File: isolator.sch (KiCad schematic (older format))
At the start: 3 parts, among them U1 Si8640BB-B-IS1

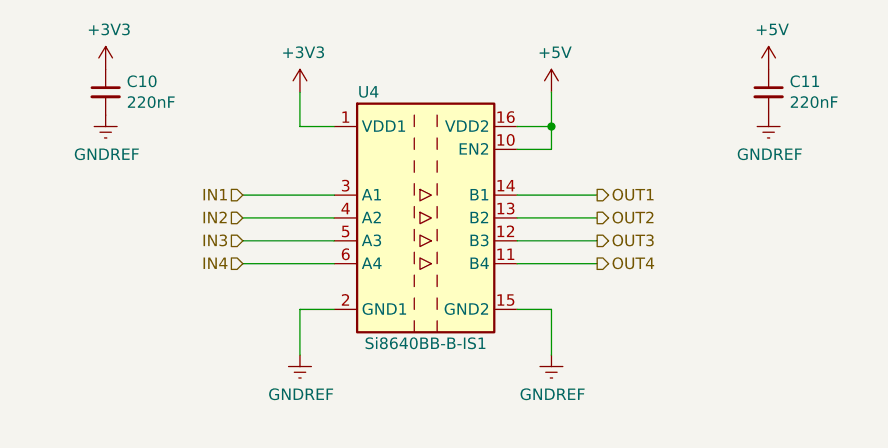
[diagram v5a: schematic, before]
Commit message: Continued layouting
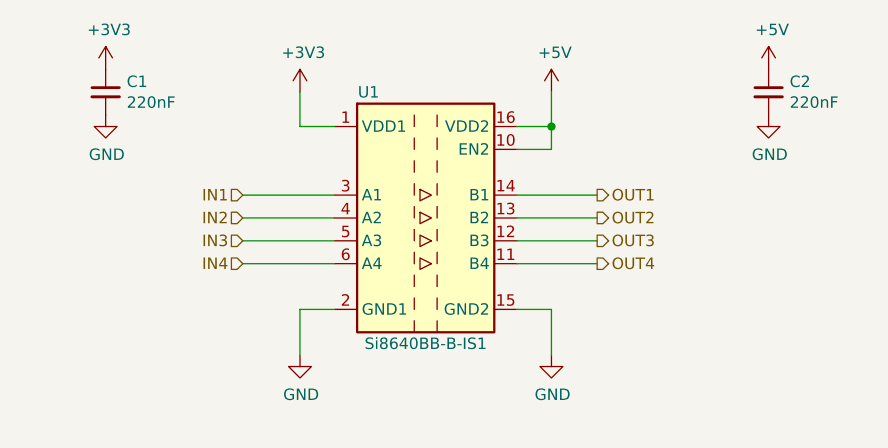
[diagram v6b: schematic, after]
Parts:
- renumbered C4 to C1, C5 to C2
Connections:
- net GNDREF renamed GND
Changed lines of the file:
@@
 P 5200 3500
 AR Path="/5BCC578B/5BCC7CBC" Ref="U1"  Part="1"
-AR Path="/5BCC79AE/5BCC7CBC" Ref="U3"  Part="1"
-AR Path="/5BCC7A96/5BCC7CBC" Ref="U2"  Part="1"
-AR Path="/5BCC8BB7/5BCC7CBC" Ref="U4"  Part="1"
-F 0 "U4" H 4950 4050 50  0000 C CNN
+AR Path="/5BCC79AE/5BCC7CBC" Ref="U4"  Part="1"
+AR Path="/5BCC7A96/5BCC7CBC" Ref="U3"  Part="1"
+AR Path="/5BCC8BB7/5BCC7CBC" Ref="U5"  Part="1"
+F 0 "U1" H 4950 4050 50  0000 C CNN
 F 1 "Si8640BB-B-IS1" H 5200 2950 50  0000 C CNN
 F 2 "Package_SO:SOIC-16_3.9x9.9mm_P1.27mm" H 5200 2950 50  0001 C CIN
@@
 $EndComp
 $Comp
-L power:GNDREF #PWR0105
-U 1 1 5BCC7D47
-P 4650 4100
-AR Path="/5BCC578B/5BCC7D47" Ref="#PWR0105"  Part="1"
-AR Path="/5BCC79AE/5BCC7D47" Ref="#PWR0118"  Part="1"
-AR Path="/5BCC7A96/5BCC7D47" Ref="#PWR0114"  Part="1"
-AR Path="/5BCC8BB7/5BCC7D47" Ref="#PWR0122"  Part="1"
-F 0 "#PWR0122" H 4650 3850 50  0001 C CNN
-F 1 "GNDREF" H 4655 3927 50  0000 C CNN
-F 2 "" H 4650 4100 50  0001 C CNN
-F 3 "" H 4650 4100 50  0001 C CNN
-	1    4650 4100
-	1    0    0    -1
-$EndComp
-$Comp
-L power:GNDREF #PWR0106
-U 1 1 5BCC7D5B
-P 5750 4100
-AR Path="/5BCC578B/5BCC7D5B" Ref="#PWR0106"  Part="1"
-AR Path="/5BCC79AE/5BCC7D5B" Ref="#PWR0119"  Part="1"
-AR Path="/5BCC7A96/5BCC7D5B" Ref="#PWR0115"  Part="1"
-AR Path="/5BCC8BB7/5BCC7D5B" Ref="#PWR0123"  Part="1"
-F 0 "#PWR0123" H 5750 3850 50  0001 C CNN
-F 1 "GNDREF" H 5755 3927 50  0000 C CNN
-F 2 "" H 5750 4100 50  0001 C CNN
-F 3 "" H 5750 4100 50  0001 C CNN
-	1    5750 4100
-	1    0    0    -1
-$EndComp
-$Comp
-L power:+3V3 #PWR0107
+L power:+3V3 #PWR07
 U 1 1 5BCC7DB8
 P 4650 2950
-AR Path="/5BCC578B/5BCC7DB8" Ref="#PWR0107"  Part="1"
-AR Path="/5BCC79AE/5BCC7DB8" Ref="#PWR0120"  Part="1"
-AR Path="/5BCC7A96/5BCC7DB8" Ref="#PWR0116"  Part="1"
-AR Path="/5BCC8BB7/5BCC7DB8" Ref="#PWR0124"  Part="1"
-F 0 "#PWR0124" H 4650 2800 50  0001 C CNN
+AR Path="/5BCC578B/5BCC7DB8" Ref="#PWR07"  Part="1"
+AR Path="/5BCC79AE/5BCC7DB8" Ref="#PWR028"  Part="1"
+AR Path="/5BCC7A96/5BCC7DB8" Ref="#PWR020"  Part="1"
+AR Path="/5BCC8BB7/5BCC7DB8" Ref="#PWR036"  Part="1"
+F 0 "#PWR07" H 4650 2800 50  0001 C CNN
 F 1 "+3V3" H 4665 3123 50  0000 C CNN
 F 2 "" H 4650 2950 50  0001 C CNN
@@
 $EndComp
 $Comp
-L power:+5V #PWR0108
+L power:+5V #PWR09
 U 1 1 5BCC7E07
 P 5750 2950
-AR Path="/5BCC578B/5BCC7E07" Ref="#PWR0108"  Part="1"
-AR Path="/5BCC79AE/5BCC7E07" Ref="#PWR0121"  Part="1"
-AR Path="/5BCC7A96/5BCC7E07" Ref="#PWR0117"  Part="1"
-AR Path="/5BCC8BB7/5BCC7E07" Ref="#PWR0125"  Part="1"
-F 0 "#PWR0125" H 5750 2800 50  0001 C CNN
+AR Path="/5BCC578B/5BCC7E07" Ref="#PWR09"  Part="1"
+AR Path="/5BCC79AE/5BCC7E07" Ref="#PWR030"  Part="1"
+AR Path="/5BCC7A96/5BCC7E07" Ref="#PWR022"  Part="1"
+AR Path="/5BCC8BB7/5BCC7E07" Ref="#PWR038"  Part="1"
+F 0 "#PWR09" H 5750 2800 50  0001 C CNN
 F 1 "+5V" H 5765 3123 50  0000 C CNN
 F 2 "" H 5750 2950 50  0001 C CNN
@@
 	5750 2950 5750 3100
 $Comp
-L power:+3V3 #PWR01
+L power:+3V3 #PWR05
 U 1 1 5BCCF224
 P 3800 2850
-AR Path="/5BCC578B/5BCCF224" Ref="#PWR01"  Part="1"
-AR Path="/5BCC79AE/5BCCF224" Ref="#PWR09"  Part="1"
-AR Path="/5BCC7A96/5BCCF224" Ref="#PWR05"  Part="1"
-AR Path="/5BCC8BB7/5BCCF224" Ref="#PWR013"  Part="1"
-F 0 "#PWR013" H 3800 2700 50  0001 C CNN
+AR Path="/5BCC578B/5BCCF224" Ref="#PWR05"  Part="1"
+AR Path="/5BCC79AE/5BCCF224" Ref="#PWR026"  Part="1"
+AR Path="/5BCC7A96/5BCCF224" Ref="#PWR018"  Part="1"
+AR Path="/5BCC8BB7/5BCCF224" Ref="#PWR034"  Part="1"
+F 0 "#PWR05" H 3800 2700 50  0001 C CNN
 F 1 "+3V3" H 3815 3023 50  0000 C CNN
 F 2 "" H 3800 2850 50  0001 C CNN
@@
 $EndComp
 $Comp
-L Device:C_Small C4
+L Device:C_Small C1
 U 1 1 5BCCF242
 P 3800 2950
-AR Path="/5BCC578B/5BCCF242" Ref="C4"  Part="1"
+AR Path="/5BCC578B/5BCCF242" Ref="C1"  Part="1"
 AR Path="/5BCC79AE/5BCCF242" Ref="C8"  Part="1"
 AR Path="/5BCC7A96/5BCCF242" Ref="C6"  Part="1"
 AR Path="/5BCC8BB7/5BCCF242" Ref="C10"  Part="1"
-F 0 "C10" H 3892 2996 50  0000 L CNN
+F 0 "C1" H 3892 2996 50  0000 L CNN
 F 1 "220nF" H 3892 2905 50  0000 L CNN
 F 2 "Capacitor_SMD:C_0805_2012Metric_Pad1.15x1.40mm_HandSolder" H 3800 2950 50  0001 C CNN
@@
 $EndComp
 $Comp
-L power:GNDREF #PWR02
-U 1 1 5BCCF276
-P 3800 3050
-AR Path="/5BCC578B/5BCCF276" Ref="#PWR02"  Part="1"
-AR Path="/5BCC79AE/5BCCF276" Ref="#PWR010"  Part="1"
-AR Path="/5BCC7A96/5BCCF276" Ref="#PWR06"  Part="1"
-AR Path="/5BCC8BB7/5BCCF276" Ref="#PWR014"  Part="1"
-F 0 "#PWR014" H 3800 2800 50  0001 C CNN
-F 1 "GNDREF" H 3805 2877 50  0000 C CNN
-F 2 "" H 3800 3050 50  0001 C CNN
-F 3 "" H 3800 3050 50  0001 C CNN
-	1    3800 3050
-	1    0    0    -1
-$EndComp
-$Comp
-L Device:C_Small C5
+L Device:C_Small C2
 U 1 1 5BCCF2B7
 P 6700 2950
-AR Path="/5BCC578B/5BCCF2B7" Ref="C5"  Part="1"
+AR Path="/5BCC578B/5BCCF2B7" Ref="C2"  Part="1"
 AR Path="/5BCC79AE/5BCCF2B7" Ref="C9"  Part="1"
 AR Path="/5BCC7A96/5BCCF2B7" Ref="C7"  Part="1"
 AR Path="/5BCC8BB7/5BCCF2B7" Ref="C11"  Part="1"
-F 0 "C11" H 6792 2996 50  0000 L CNN
+F 0 "C2" H 6792 2996 50  0000 L CNN
 F 1 "220nF" H 6792 2905 50  0000 L CNN
 F 2 "Capacitor_SMD:C_0805_2012Metric_Pad1.15x1.40mm_HandSolder" H 6700 2950 50  0001 C CNN
@@
 $EndComp
 $Comp
-L power:+5V #PWR03
+L power:+5V #PWR011
 U 1 1 5BCCF324
 P 6700 2850
-AR Path="/5BCC578B/5BCCF324" Ref="#PWR03"  Part="1"
-AR Path="/5BCC79AE/5BCCF324" Ref="#PWR011"  Part="1"
-AR Path="/5BCC7A96/5BCCF324" Ref="#PWR07"  Part="1"
-AR Path="/5BCC8BB7/5BCCF324" Ref="#PWR015"  Part="1"
-F 0 "#PWR015" H 6700 2700 50  0001 C CNN
+AR Path="/5BCC578B/5BCCF324" Ref="#PWR011"  Part="1"
+AR Path="/5BCC79AE/5BCCF324" Ref="#PWR032"  Part="1"
+AR Path="/5BCC7A96/5BCCF324" Ref="#PWR024"  Part="1"
+AR Path="/5BCC8BB7/5BCCF324" Ref="#PWR040"  Part="1"
+F 0 "#PWR011" H 6700 2700 50  0001 C CNN
 F 1 "+5V" H 6715 3023 50  0000 C CNN
 F 2 "" H 6700 2850 50  0001 C CNN
@@
 $EndComp
 $Comp
-L power:GNDREF #PWR04
-U 1 1 5BCCF348
+L power:GND #PWR06
+U 1 1 5BCF7281
+P 3800 3050
+AR Path="/5BCC578B/5BCF7281" Ref="#PWR06"  Part="1"
+AR Path="/5BCC7A96/5BCF7281" Ref="#PWR019"  Part="1"
+AR Path="/5BCC79AE/5BCF7281" Ref="#PWR027"  Part="1"
+AR Path="/5BCC8BB7/5BCF7281" Ref="#PWR035"  Part="1"
+F 0 "#PWR06" H 3800 2800 50  0001 C CNN
+F 1 "GND" H 3805 2877 50  0000 C CNN
+F 2 "" H 3800 3050 50  0001 C CNN
+F 3 "" H 3800 3050 50  0001 C CNN
+	1    3800 3050
+	1    0    0    -1
+$EndComp
+$Comp
+L power:GND #PWR08
+U 1 1 5BCF7299
+P 4650 4100
+AR Path="/5BCC578B/5BCF7299" Ref="#PWR08"  Part="1"
+AR Path="/5BCC7A96/5BCF7299" Ref="#PWR021"  Part="1"
+AR Path="/5BCC79AE/5BCF7299" Ref="#PWR029"  Part="1"
+AR Path="/5BCC8BB7/5BCF7299" Ref="#PWR037"  Part="1"
+F 0 "#PWR08" H 4650 3850 50  0001 C CNN
+F 1 "GND" H 4655 3927 50  0000 C CNN
+F 2 "" H 4650 4100 50  0001 C CNN
+F 3 "" H 4650 4100 50  0001 C CNN
+	1    4650 4100
+	1    0    0    -1
+$EndComp
+$Comp
+L power:GND #PWR010
+U 1 1 5BCF72AA
+P 5750 4100
+AR Path="/5BCC578B/5BCF72AA" Ref="#PWR010"  Part="1"
+AR Path="/5BCC7A96/5BCF72AA" Ref="#PWR023"  Part="1"
+AR Path="/5BCC79AE/5BCF72AA" Ref="#PWR031"  Part="1"
+AR Path="/5BCC8BB7/5BCF72AA" Ref="#PWR039"  Part="1"
+F 0 "#PWR010" H 5750 3850 50  0001 C CNN
+F 1 "GND" H 5755 3927 50  0000 C CNN
+F 2 "" H 5750 4100 50  0001 C CNN
+F 3 "" H 5750 4100 50  0001 C CNN
+	1    5750 4100
+	1    0    0    -1
+$EndComp
+$Comp
+L power:GND #PWR012
+U 1 1 5BCF72BB
 P 6700 3050
-AR Path="/5BCC578B/5BCCF348" Ref="#PWR04"  Part="1"
-AR Path="/5BCC79AE/5BCCF348" Ref="#PWR012"  Part="1"
-AR Path="/5BCC7A96/5BCCF348" Ref="#PWR08"  Part="1"
-AR Path="/5BCC8BB7/5BCCF348" Ref="#PWR016"  Part="1"
-F 0 "#PWR016" H 6700 2800 50  0001 C CNN
-F 1 "GNDREF" H 6705 2877 50  0000 C CNN
+AR Path="/5BCC578B/5BCF72BB" Ref="#PWR012"  Part="1"
+AR Path="/5BCC7A96/5BCF72BB" Ref="#PWR025"  Part="1"
+AR Path="/5BCC79AE/5BCF72BB" Ref="#PWR033"  Part="1"
+AR Path="/5BCC8BB7/5BCF72BB" Ref="#PWR041"  Part="1"
+F 0 "#PWR012" H 6700 2800 50  0001 C CNN
+F 1 "GND" H 6705 2877 50  0000 C CNN
 F 2 "" H 6700 3050 50  0001 C CNN
 F 3 "" H 6700 3050 50  0001 C CNN

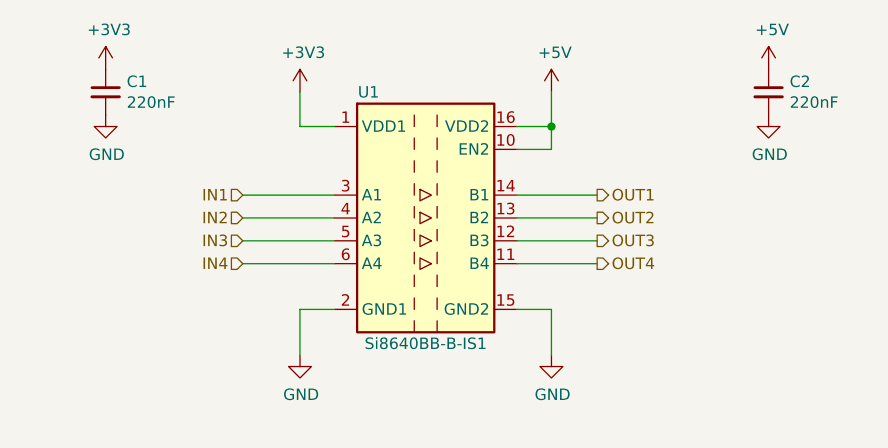
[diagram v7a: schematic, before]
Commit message: Switched to Si8660 isolator and changed RJ-45 connector
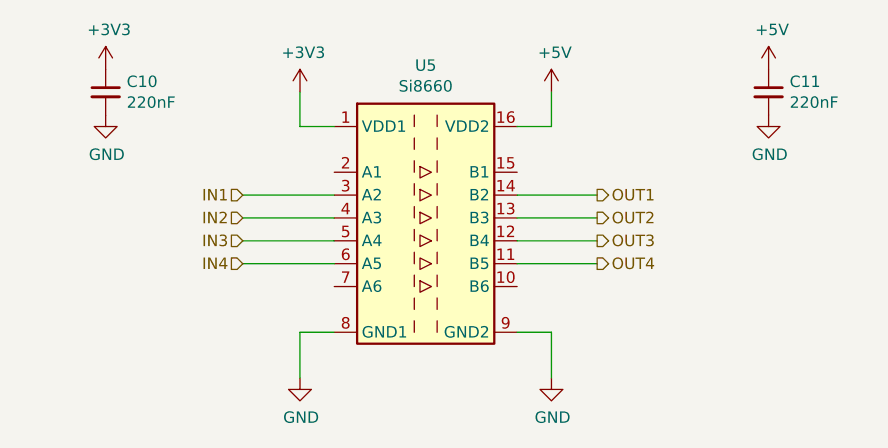
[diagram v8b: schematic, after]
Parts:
- removed U1: Si8640BB-B-IS1, Package_SO:SOIC-16_3.9x9.9mm_P1.27mm, symbol Isolator:Si8640BB-B-IS1
- added U1: Si8660, Package_SO:SOIC-16_3.9x9.9mm_P1.27mm, symbol Matthias:Si8660
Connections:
- net +3V3: now also U1.1 (VDD1)
- net +5V: now also U1.16 (VDD2)
- net GND: now also U1.8 (GND1), U1.9 (GND2)
- net IN1: now also U1.3 (A2)
- net IN2: now also U1.4 (A3)
- net IN3: now also U1.5 (A4)
- net IN4: now also U1.6 (A5)
- net OUT1: now also U1.14 (B2)
- net OUT2: now also U1.13 (B3)
- net OUT3: now also U1.12 (B4)
- net OUT4: now also U1.11 (B5)
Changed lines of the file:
@@
 $Descr A4 11693 8268
 encoding utf-8
-Sheet 3 11
+Sheet 6 11
 Title ""
 Date ""
@@
 OUT4
 $Comp
-L Isolator:Si8640BB-B-IS1 U1
-U 1 1 5BCC7CBC
-P 5200 3500
-AR Path="/5BCC578B/5BCC7CBC" Ref="U1"  Part="1"
-AR Path="/5BCC79AE/5BCC7CBC" Ref="U4"  Part="1"
-AR Path="/5BCC7A96/5BCC7CBC" Ref="U3"  Part="1"
-AR Path="/5BCC8BB7/5BCC7CBC" Ref="U5"  Part="1"
-F 0 "U1" H 4950 4050 50  0000 C CNN
-F 1 "Si8640BB-B-IS1" H 5200 2950 50  0000 C CNN
-F 2 "Package_SO:SOIC-16_3.9x9.9mm_P1.27mm" H 5200 2950 50  0001 C CIN
-F 3 "https://www.silabs.com/documents/public/data-sheets/si864x-datasheet.pdf" H 5200 3900 50  0001 C CNN
-	1    5200 3500
-	1    0    0    -1
-$EndComp
-$Comp
 L power:+3V3 #PWR07
 U 1 1 5BCC7DB8
@@
 	5600 3100 5750 3100
 Wire Wire Line
-	5600 3200 5750 3200
-Wire Wire Line
-	5750 3200 5750 3100
-Connection ~ 5750 3100
-Wire Wire Line
 	5600 3400 5950 3400
 Wire Wire Line
@@
 	5600 3700 5950 3700
 Wire Wire Line
-	5600 3900 5750 3900
-Wire Wire Line
-	5750 3900 5750 4100
+	5600 4000 5750 4000
+Wire Wire Line
+	5750 4000 5750 4200
 Wire Wire Line
 	4800 3100 4650 3100
@@
 	4650 3100 4650 2950
 Wire Wire Line
-	4650 4100 4650 3900
-Wire Wire Line
-	4650 3900 4800 3900
+	4650 4200 4650 4000
+Wire Wire Line
+	4650 4000 4800 4000
 Wire Wire Line
 	4800 3700 4400 3700
@@
 AR Path="/5BCC7A96/5BCCF242" Ref="C6"  Part="1"
 AR Path="/5BCC8BB7/5BCCF242" Ref="C10"  Part="1"
-F 0 "C1" H 3892 2996 50  0000 L CNN
+F 0 "C10" H 3892 2996 50  0000 L CNN
 F 1 "220nF" H 3892 2905 50  0000 L CNN
 F 2 "Capacitor_SMD:C_0805_2012Metric_Pad1.15x1.40mm_HandSolder" H 3800 2950 50  0001 C CNN
@@
 AR Path="/5BCC7A96/5BCCF2B7" Ref="C7"  Part="1"
 AR Path="/5BCC8BB7/5BCCF2B7" Ref="C11"  Part="1"
-F 0 "C2" H 6792 2996 50  0000 L CNN
+F 0 "C11" H 6792 2996 50  0000 L CNN
 F 1 "220nF" H 6792 2905 50  0000 L CNN
 F 2 "Capacitor_SMD:C_0805_2012Metric_Pad1.15x1.40mm_HandSolder" H 6700 2950 50  0001 C CNN
@@
 L power:GND #PWR08
 U 1 1 5BCF7299
-P 4650 4100
+P 4650 4200
 AR Path="/5BCC578B/5BCF7299" Ref="#PWR08"  Part="1"
 AR Path="/5BCC7A96/5BCF7299" Ref="#PWR021"  Part="1"
 AR Path="/5BCC79AE/5BCF7299" Ref="#PWR029"  Part="1"
 AR Path="/5BCC8BB7/5BCF7299" Ref="#PWR037"  Part="1"
-F 0 "#PWR037" H 4650 3850 50  0001 C CNN
-F 1 "GND" H 4655 3927 50  0000 C CNN
-F 2 "" H 4650 4100 50  0001 C CNN
-F 3 "" H 4650 4100 50  0001 C CNN
-	1    4650 4100
+F 0 "#PWR037" H 4650 3950 50  0001 C CNN
+F 1 "GND" H 4655 4027 50  0000 C CNN
+F 2 "" H 4650 4200 50  0001 C CNN
+F 3 "" H 4650 4200 50  0001 C CNN
+	1    4650 4200
 	1    0    0    -1
 $EndComp
@@
 L power:GND #PWR010
 U 1 1 5BCF72AA
-P 5750 4100
+P 5750 4200
 AR Path="/5BCC578B/5BCF72AA" Ref="#PWR010"  Part="1"
 AR Path="/5BCC7A96/5BCF72AA" Ref="#PWR023"  Part="1"
 AR Path="/5BCC79AE/5BCF72AA" Ref="#PWR031"  Part="1"
 AR Path="/5BCC8BB7/5BCF72AA" Ref="#PWR039"  Part="1"
-F 0 "#PWR039" H 5750 3850 50  0001 C CNN
-F 1 "GND" H 5755 3927 50  0000 C CNN
-F 2 "" H 5750 4100 50  0001 C CNN
-F 3 "" H 5750 4100 50  0001 C CNN
-	1    5750 4100
+F 0 "#PWR039" H 5750 3950 50  0001 C CNN
+F 1 "GND" H 5755 4027 50  0000 C CNN
+F 2 "" H 5750 4200 50  0001 C CNN
+F 3 "" H 5750 4200 50  0001 C CNN
+	1    5750 4200
 	1    0    0    -1
 $EndComp
@@
 	1    0    0    -1
 $EndComp
+$Comp
+L Matthias:Si8660 U1
+U 1 1 5BE0D51C
+P 5200 3500
+AR Path="/5BCC578B/5BE0D51C" Ref="U1"  Part="1"
+AR Path="/5BCC7A96/5BE0D51C" Ref="U3"  Part="1"
+AR Path="/5BCC79AE/5BE0D51C" Ref="U4"  Part="1"
+AR Path="/5BCC8BB7/5BE0D51C" Ref="U5"  Part="1"
+F 0 "U5" H 5200 4167 50  0000 C CNN
+F 1 "Si8660" H 5200 4076 50  0000 C CNN
+F 2 "Package_SO:SOIC-16_3.9x9.9mm_P1.27mm" H 5200 2850 50  0001 C CIN
+F 3 "" H 5200 3900 50  0001 C CNN
+	1    5200 3500
+	1    0    0    -1
+$EndComp
